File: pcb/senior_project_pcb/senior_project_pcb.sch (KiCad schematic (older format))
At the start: 0 parts

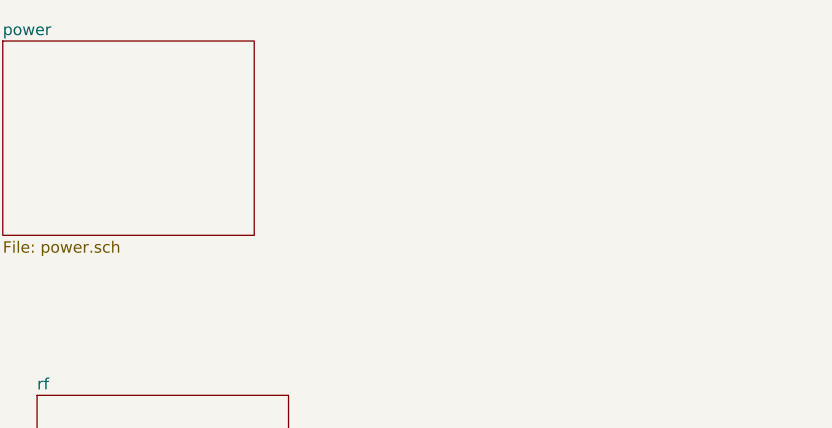
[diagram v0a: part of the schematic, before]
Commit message: Add pulse oximeter circuit
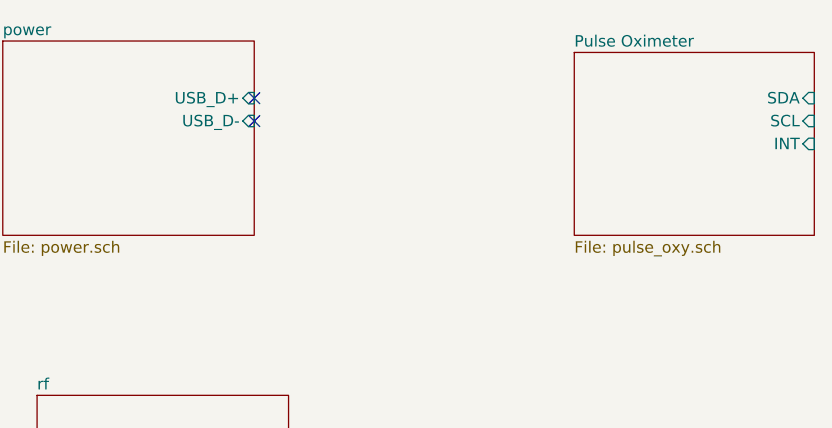
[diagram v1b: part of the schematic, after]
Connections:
- no-connect marks 0 -> 2
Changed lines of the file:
@@
 $Descr A4 11693 8268
 encoding utf-8
-Sheet 1 4
+Sheet 1 5
 Title ""
 Date ""
@@
 F0 "power" 50
 F1 "power.sch" 50
+F2 "USB_D+" I R 3550 2400 50
+F3 "USB_D-" I R 3550 2500 50
 $EndSheet
 $Sheet
@@
 F1 "io.sch" 50
 $EndSheet
+$Sheet
+S 4950 2200 1050 800
+U 601C9014
+F0 "Pulse Oximeter" 50
+F1 "pulse_oxy.sch" 50
+F2 "SDA" I R 6000 2400 50
+F3 "SCL" I R 6000 2500 50
+F4 "INT" I R 6000 2600 50
+$EndSheet
+NoConn ~ 3550 2400
+NoConn ~ 3550 2500
 $EndSCHEMATC

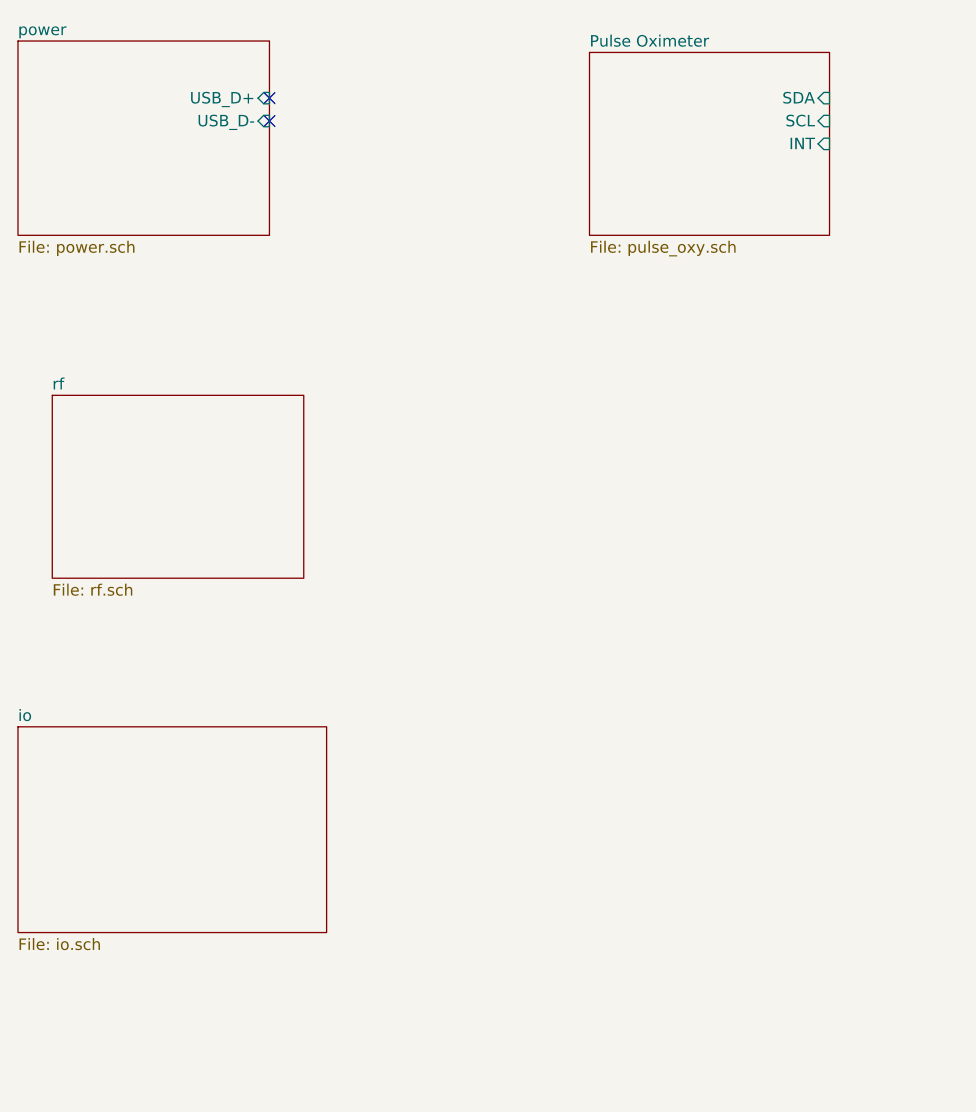
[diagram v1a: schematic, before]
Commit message: Connect up the pulse oximeter and USB
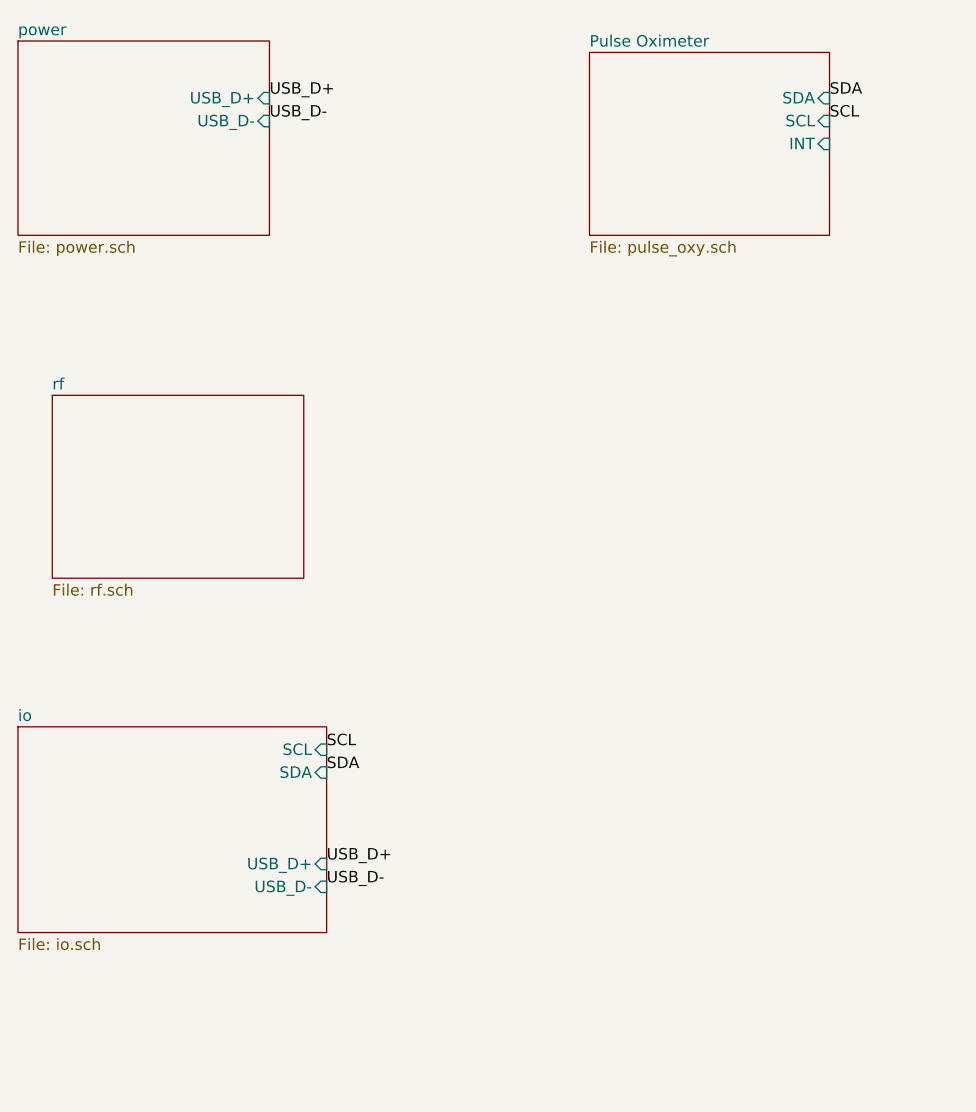
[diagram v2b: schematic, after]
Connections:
- no-connect marks 2 -> 0
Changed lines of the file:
@@
 F0 "io" 50
 F1 "io.sch" 50
+F2 "SCL" I R 3800 5250 50
+F3 "SDA" I R 3800 5350 50
+F4 "USB_D+" I R 3800 5750 50
+F5 "USB_D-" I R 3800 5850 50
 $EndSheet
 $Sheet
@@
 F4 "INT" I R 6000 2600 50
 $EndSheet
-NoConn ~ 3550 2400
-NoConn ~ 3550 2500
+Text Label 6000 2400 0    50   ~ 0
+SDA
+Text Label 3800 5250 0    50   ~ 0
+SCL
+Text Label 3800 5350 0    50   ~ 0
+SDA
+Text Label 6000 2500 0    50   ~ 0
+SCL
+Text Label 3800 5750 0    50   ~ 0
+USB_D+
+Text Label 3550 2400 0    50   ~ 0
+USB_D+
+Text Label 3800 5850 0    50   ~ 0
+USB_D-
+Text Label 3550 2500 0    50   ~ 0
+USB_D-
 $EndSCHEMATC

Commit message: Add temp sensor
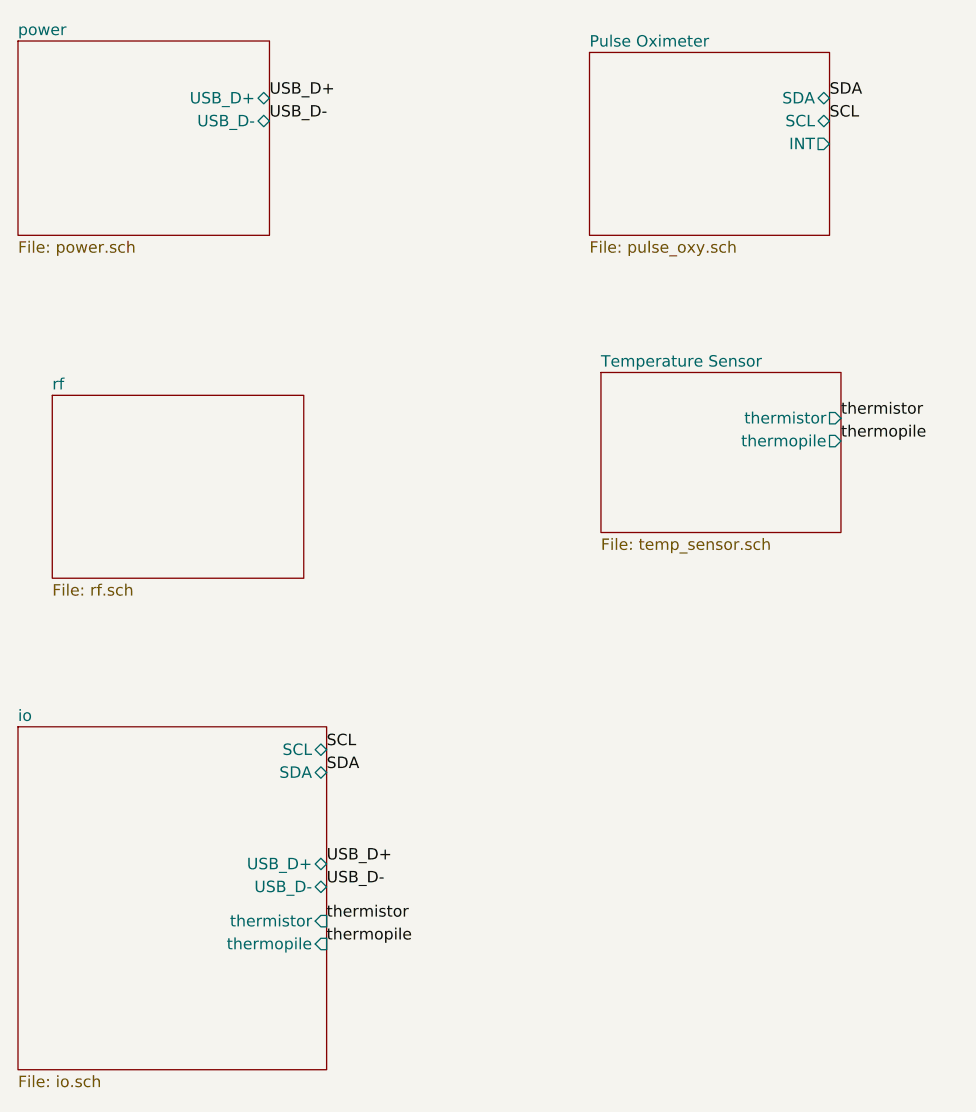
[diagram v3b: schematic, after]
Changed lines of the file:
@@
 $Descr A4 11693 8268
 encoding utf-8
-Sheet 1 5
+Sheet 1 6
 Title ""
 Date ""
@@
 F0 "power" 50
 F1 "power.sch" 50
-F2 "USB_D+" I R 3550 2400 50
-F3 "USB_D-" I R 3550 2500 50
+F2 "USB_D+" B R 3550 2400 50
+F3 "USB_D-" B R 3550 2500 50
 $EndSheet
 $Sheet
@@
 $EndSheet
 $Sheet
-S 2450 5150 1350 900
-U 5FC31852
-F0 "io" 50
-F1 "io.sch" 50
-F2 "SCL" I R 3800 5250 50
-F3 "SDA" I R 3800 5350 50
-F4 "USB_D+" I R 3800 5750 50
-F5 "USB_D-" I R 3800 5850 50
-$EndSheet
-$Sheet
 S 4950 2200 1050 800
 U 601C9014
 F0 "Pulse Oximeter" 50
 F1 "pulse_oxy.sch" 50
-F2 "SDA" I R 6000 2400 50
-F3 "SCL" I R 6000 2500 50
-F4 "INT" I R 6000 2600 50
+F2 "SDA" B R 6000 2400 50
+F3 "SCL" B R 6000 2500 50
+F4 "INT" O R 6000 2600 50
 $EndSheet
 Text Label 6000 2400 0    50   ~ 0
@@
 Text Label 3550 2500 0    50   ~ 0
 USB_D-
+$Sheet
+S 5000 3600 1050 700
+U 60146A6B
+F0 "Temperature Sensor" 50
+F1 "temp_sensor.sch" 50
+F2 "thermistor" O R 6050 3800 50
+F3 "thermopile" O R 6050 3900 50
+$EndSheet
+$Sheet
+S 2450 5150 1350 1500
+U 5FC31852
+F0 "io" 50
+F1 "io.sch" 50
+F2 "SCL" B R 3800 5250 50
+F3 "SDA" B R 3800 5350 50
+F4 "USB_D+" B R 3800 5750 50
+F5 "USB_D-" B R 3800 5850 50
+F6 "thermistor" I R 3800 6000 50
+F7 "thermopile" I R 3800 6100 50
+$EndSheet
+Text Label 6050 3800 0    50   ~ 0
+thermistor
+Text Label 3800 6000 0    50   ~ 0
+thermistor
+Text Label 3800 6100 0    50   ~ 0
+thermopile
+Text Label 6050 3900 0    50   ~ 0
+thermopile
 $EndSCHEMATC

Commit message: Initial layout mostly done
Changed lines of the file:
@@
 F6 "thermistor" I R 3800 6000 50
 F7 "thermopile" I R 3800 6100 50
+F8 "INT" I R 3800 5450 50
 $EndSheet
 Text Label 6050 3800 0    50   ~ 0
@@
 Text Label 6050 3900 0    50   ~ 0
 thermopile
+Text Label 3800 5450 0    50   ~ 0
+INT
+Text Label 6000 2600 0    50   ~ 0
+INT
 $EndSCHEMATC

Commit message: Add ecg sensor
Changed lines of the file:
@@
 EESchema Schematic File Version 4
-EELAYER 30 0
+LIBS:senior_project_pcb-cache
+EELAYER 29 0
 EELAYER END
 $Descr A4 11693 8268
 encoding utf-8
-Sheet 1 6
+Sheet 1 7
 Title ""
 Date ""
@@
 Text Label 6000 2600 0    50   ~ 0
 INT
+$Sheet
+S 4950 5000 1150 900
+U 602C4640
+F0 "ecg" 50
+F1 "ecg.sch" 50
+$EndSheet
 $EndSCHEMATC

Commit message: Add RF/Bluetooth to PCB
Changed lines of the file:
@@
 EESchema Schematic File Version 4
-LIBS:senior_project_pcb-cache
-EELAYER 29 0
+EELAYER 30 0
 EELAYER END
 $Descr A4 11693 8268
@@
 F7 "thermopile" I R 3800 6100 50
 F8 "INT" I R 3800 5450 50
+F9 "ECG_OUT" I R 3800 6300 50
+F10 "ECG_SDN" I R 3800 6400 50
 $EndSheet
 Text Label 6050 3800 0    50   ~ 0
@@
 F0 "ecg" 50
 F1 "ecg.sch" 50
+F2 "ECG_OUT" O R 6100 5150 50
+F3 "ECG_SDN" I R 6100 5250 50
 $EndSheet
+Text Label 3800 6300 0    50   ~ 0
+ECG_OUT
+Text Label 6100 5150 0    50   ~ 0
+ECG_OUT
+Text Label 6100 5250 0    50   ~ 0
+ECG_SDN
+Text Label 3800 6400 0    50   ~ 0
+ECG_SDN
 $EndSCHEMATC

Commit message: PCB Update
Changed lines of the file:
@@
 F9 "ECG_OUT" I R 3800 6300 50
 F10 "ECG_SDN" I R 3800 6400 50
+F11 "LO+" I R 3800 6500 50
+F12 "LO-" I R 3800 6600 50
 $EndSheet
 Text Label 6050 3800 0    50   ~ 0
@@
 F2 "ECG_OUT" O R 6100 5150 50
 F3 "ECG_SDN" I R 6100 5250 50
+F4 "LO+" O R 6100 5450 50
+F5 "LO-" O R 6100 5550 50
 $EndSheet
 Text Label 3800 6300 0    50   ~ 0
@@
 Text Label 3800 6400 0    50   ~ 0
 ECG_SDN
+Text Label 3800 6500 0    50   ~ 0
+LO+
+Text Label 6100 5450 0    50   ~ 0
+LO+
+Text Label 6100 5550 0    50   ~ 0
+LO-
+Text Label 3800 6600 0    50   ~ 0
+LO-
 $EndSCHEMATC
